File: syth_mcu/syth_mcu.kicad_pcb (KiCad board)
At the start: 2 copper layers, 138 x 121 mm, 33 parts, among them J1 USB_C_Receptacle_PowerOnly_6P, J2 Conn_01x05, J3 Conn_01x05, SW1 SW_Push, SW2 SW_Push, SW3 SW_Push, SW4 SW_Push, SW5 SW_Push, U1 TFT_320x240, U2 YAAJ_WeAct_BlackPill_Part_Like, U3 74HC4051, U4 AMS1117-3.3, U5 AMS1117-3.3

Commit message: kicad: widen board for 12-key hall row, wire DAC power, footprint fixes
- Edge.Cuts resized 167x94.5 -> 286x133mm to fit 12 real-pitch (23mm)
  hall-effect key positions below the control row
- H1-H12 mounting holes shifted to new bottom edge
- add dac-pchannel.kicad_sch as tracked sheet file (was external ref)
- C1/C2 footprint corrected to non-polarized box-film C_Rect
- misc footprint/placement fixes from Cream Bun review pass
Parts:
- added C1: 80nF, Capacitor_THT:CP_Radial_D4.0mm_P2.00mm, F.Cu at (211.7, 53.8)
- added C2: 80nF, Capacitor_THT:CP_Radial_D4.0mm_P2.00mm, F.Cu at (202.9, 70.4)
- added C3: 0.1uF C, Capacitor_THT:C_Disc_D5.0mm_W2.5mm_P2.50mm, F.Cu at (163.2, 69.4)
- added C4: 0.1uF C, Capacitor_THT:C_Disc_D5.0mm_W2.5mm_P2.50mm, F.Cu at (163.2, 62.9)
- added C5: 1uF, Capacitor_THT:C_Rect_L9.0mm_W3.2mm_P7.50mm_MKT, F.Cu at (209.2, 28.4)
- added C6: 33uF, Capacitor_THT:CP_Radial_D4.0mm_P2.00mm, F.Cu at (216.7, 53.8)
- added C7: 1uF, Capacitor_THT:C_Rect_L9.0mm_W3.2mm_P7.50mm_MKT, F.Cu at (167.7, 64.9)
- added C8: 33uF, Capacitor_THT:CP_Radial_D4.0mm_P2.00mm, F.Cu at (216.2, 75.3)
- added J4: AudioPlug3, Connector_Audio:Jack_3.5mm_CUI_SJ1-3533NG_Horizontal, F.Cu at (229.2, 26.1)
- added Q1: SI2307DS, Package_TO_SOT_SMD:SOT-23, F.Cu at (217.3, 37.8)
- added Q2: SI2304DS, Package_TO_SOT_SMD:SOT-23, F.Cu at (211.7, 37.6)
- added Q3: SI2307DS, Package_TO_SOT_SMD:SOT-23, F.Cu at (215.7, 67.9)
- added Q4: SI2304DS, Package_TO_SOT_SMD:SOT-23, F.Cu at (215.7, 63.1)
- added R10: 10k, Resistor_THT:R_Axial_DIN0207_L6.3mm_D2.5mm_P10.16mm_Horizontal, F.Cu at (211.9, 78.4)
- added R3: 10k, Resistor_THT:R_Axial_DIN0207_L6.3mm_D2.5mm_P10.16mm_Horizontal, F.Cu at (205.7, 42.9)
- added R4: 10k, Resistor_THT:R_Axial_DIN0207_L6.3mm_D2.5mm_P10.16mm_Horizontal, F.Cu at (210.7, 60.4)
- added R5: 2k, Resistor_THT:R_Axial_DIN0207_L6.3mm_D2.5mm_P10.16mm_Horizontal, F.Cu at (202.2, 32.7)
- added R6: 2k, Resistor_THT:R_Axial_DIN0207_L6.3mm_D2.5mm_P10.16mm_Horizontal, F.Cu at (209.2, 32.8)
- added R7: 100 1%, Resistor_THT:R_Axial_DIN0207_L6.3mm_D2.5mm_P10.16mm_Horizontal, F.Cu at (209.2, 43.8)
- added R8: 100 1%, Resistor_THT:R_Axial_DIN0207_L6.3mm_D2.5mm_P10.16mm_Horizontal, F.Cu at (211.9, 74.8)
- added R9: 10k, Resistor_THT:R_Axial_DIN0207_L6.3mm_D2.5mm_P10.16mm_Horizontal, F.Cu at (209.2, 47.8)
- added RV6: 100k, Potentiometer_THT:Potentiometer_Bourns_3296W_Vertical, F.Cu at (203.3, 47.3)
- added RV7: 100k, Potentiometer_THT:Potentiometer_Bourns_3296W_Vertical, F.Cu at (203.3, 58.3)
- U5: renamed from U1; moved to B.Cu
- moved R2 131.5 mm to (168.4, 29.6), turned to -90 degrees
- moved R1 125.3 mm to (162.9, 29.6), turned to -90 degrees
- moved D1 124.0 mm to (165.9, 25.3), turned to 0 degrees
- moved H11 122.2 mm to (284.7, 144.5)
- moved J1 116.4 mm to (292.7, 60.8)
- moved H9 106.7 mm to (260.6, 144.5)
- moved J3 106.2 mm to (20.0, 25.5), turned to 180 degrees
- moved U3 102.3 mm to (165.6, 47.5), turned to 180 degrees
- moved H7 91.3 mm to (236.4, 144.5)
- moved U4 87.9 mm to (165.6, 56.8), turned to 180 degrees
- moved H5 75.9 mm to (212.2, 144.5)
- moved U6 74.6 mm to (194.0, 78.0)
- moved H12 60.6 mm to (188.0, 144.5)
- moved H2 57.5 mm to (18.7, 144.5)
- moved J2 55.1 mm to (10.7, 60.8)
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- renumbered H7 to H10, H12 to H11, H8 to H12, H9 to H5, H5 to H6, H10 to H7, H6 to H8, H11 to H9, J3 to J1, J1 to J3, R3 to R1, R4 to R2, U4 to U3, U5 to U4, U3 to U6
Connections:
- U2 pad 11: unconnected-(U2-PB3-Pad11) -> PB3
- U2 pad 32: unconnected-(U2-PA6-Pad32) -> PA6
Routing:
- net GND: track 448.8 -> 0.00 mm, vias 3 -> 0
- net AMS1_3.3V: track 254.4 -> 0.00 mm, vias 1 -> 0
- net D_5V: track 220.0 -> 0.00 mm, vias 3 -> 0
- net PA0: track 172.2 -> 0.00 mm
- net PA1: track 164.2 -> 0.00 mm
- net PB7: track 157.9 -> 0.00 mm
- net PA2: track 150.3 -> 0.00 mm
- net PB6: track 147.7 -> 0.00 mm, vias 1 -> 0
- net PB2: track 145.6 -> 0.00 mm, vias 1 -> 0
- net PA3: track 142.3 -> 0.00 mm
- net PB4: track 124.7 -> 0.00 mm, vias 1 -> 0
- net PA11: track 115.4 -> 0.00 mm
- net PB1: track 113.7 -> 0.00 mm
- net PB0: track 108.7 -> 0.00 mm
- net AMS2_3.3V: track 94.6 -> 0.00 mm, vias 1 -> 0
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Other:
- board size 138 x 121 mm -> 286 x 133 mm

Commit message: update layout
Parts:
- removed H1, H2, H3, H4, H5: ~, Package_TO_SOT_THT:TO-92_Inline
- removed U6: 74HC4051, Package_DIP:DIP-16_W7.62mm
- added J5: Conn_01x20, Connector_PinSocket_2.54mm:PinSocket_1x20_P2.54mm_Vertical, F.Cu at (252.4, 22.8)
- added J6: Conn_01x20, Connector_PinSocket_2.54mm:PinSocket_1x20_P2.54mm_Vertical, F.Cu at (281.6, 22.8)
- added J7: Conn_01x16, Connector_PinSocket_2.54mm:PinSocket_1x16_P2.54mm_Vertical, B.Cu at (277.4, 101.3)
- added J8: Conn_01x08, Connector_PinSocket_2.54mm:PinSocket_1x08_P2.54mm_Vertical, B.Cu at (277.4, 80.2)
- added J9: Conn_01x07, Connector_PinSocket_2.54mm:PinSocket_1x07_P2.54mm_Vertical, F.Cu at (187.5, 102.4)
- SW1, SW2, SW3, SW4, SW5: footprint Button_Switch_THT:SW_PUSH_6mm -> Button_Switch_Keyboard:SW_Cherry_MX_1.00u_PCB
- U5: footprint YAAJ_Pills:TFT-320x240 -> Connector_PinHeader_2.54mm:PinHeader_1x14_P2.54mm_Vertical; moved to F.Cu
- moved J3 187.0 mm to (207.0, 25.9)
- moved J2 170.9 mm to (160.6, 143.0), turned to 0 degrees
- moved H6 149.9 mm to (265.2, 138.0)
- moved RV1 142.9 mm to (162.9, 26.8), turned to 0 degrees
- moved SW1 122.4 mm to (154.3, 68.8), turned to -90 degrees
- moved RV2 117.9 mm to (162.9, 44.6), turned to 0 degrees
- moved SW2 113.6 mm to (154.5, 49.8), turned to -90 degrees
- moved SW3 110.5 mm to (154.4, 30.7), turned to -90 degrees
- moved U4 108.7 mm to (224.0, -34.9)
- moved C3 97.7 mm to (238.5, 7.23)
- moved C8 97.0 mm to (228.5, -20.9), turned to 0 degrees
- moved H12 96.7 mm to (284.7, 144.5)
- moved C2 96.3 mm to (233.5, -20.9), turned to 0 degrees
- moved Q3 94.5 mm to (230.5, -25.4)
- moved R10 94.1 mm to (220.0, -15.3), turned to 90 degrees
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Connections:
- C1 pad 2: GND -> ENN
- C2 pad 2: GND -> ENN
- C3 pad 2: GND -> ENN
- C4 pad 2: GND -> ENN
- C5 pad 2: GND -> ENN
- C7 pad 2: GND -> ENN
- H10 pad 1: AMS1_3.3V -> ENN
- H10 pad 2: GND -> AMS1_3.3V
- H10 pad 3: Net-(H10-OUT) -> C9
- H11 pad 1: AMS1_3.3V -> ENN
- H11 pad 2: GND -> AMS1_3.3V
- H11 pad 3: PA3 -> C10
- H12 pad 1: AMS1_3.3V -> ENN
- H12 pad 2: GND -> AMS1_3.3V
- H12 pad 3: Net-(H12-OUT) -> C11
- H6 pad 2: GND -> ENN
- H6 pad 3: Net-(H6-OUT) -> C5
- H7 pad 2: GND -> ENN
- H7 pad 3: PA1 -> C6
- H8 pad 2: GND -> ENN
- H8 pad 3: Net-(H8-OUT) -> C7
- H9 pad 1: AMS1_3.3V -> ENN
- H9 pad 2: GND -> AMS1_3.3V
- H9 pad 3: PA2 -> C8
- J1 pad 2: GND -> ENN
- J2 pad 2: GND -> ENN
- J3 pad A12: GND -> ENN
- J3 pad B12: GND -> ENN
- J4 pad S: GND -> ENN
- Q2 pad 3: GND -> ENN
- Q4 pad 3: GND -> ENN
- R1 pad 2: GND -> ENN
- R10 pad 1: GND -> ENN
- R2 pad 2: GND -> ENN
- R3 pad 1: GND -> ENN
- R4 pad 1: GND -> ENN
- R4 pad 2: PA6 -> PA15
- R6 pad 1: PA6 -> PA15
- R9 pad 1: GND -> ENN
- RV1 pad 3: GND -> ENN
- RV2 pad 3: GND -> ENN
- RV3 pad 3: GND -> ENN
- RV4 pad 3: GND -> ENN
- RV5 pad 3: GND -> ENN
- RV6 pad 3: GND -> ENN
- RV7 pad 3: GND -> ENN
- SW1 pad 1: GND -> ENN
- SW2 pad 1: GND -> ENN
- SW3 pad 1: GND -> ENN
- SW4 pad 1: GND -> ENN
- SW5 pad 1: GND -> ENN
- U2 pad 10: unconnected-(U2-PA15-Pad10) -> PA15
- U2 pad 18: unconnected-(U2-5V-Pad18) -> D_5V
- U2 pad 19: unconnected-(U2-GND-Pad19) -> ENN
- U2 pad 2: unconnected-(U2-PB13-Pad2) -> PB13
- U2 pad 20: unconnected-(U2-3V3-Pad20) -> 3V3
- U2 pad 21: unconnected-(U2-VBat-Pad21) -> VBat
- U2 pad 22: unconnected-(U2-PC13-Pad22) -> PC13
- U2 pad 23: unconnected-(U2-PC14-Pad23) -> PC14
- U2 pad 24: unconnected-(U2-PC15-Pad24) -> PC15
- U2 pad 25: unconnected-(U2-RES-Pad25) -> RES
- U2 pad 3: unconnected-(U2-PB14-Pad3) -> PB14
- U2 pad 37: unconnected-(U2-PB10-Pad37) -> PB10
- U2 pad 38: unconnected-(U2-3V3-Pad38) -> 3V3
- U2 pad 39: GND -> ENN
- U2 pad 4: unconnected-(U2-PB15-Pad4) -> PB15
- U3 pad 1: GND -> ENN
- U4 pad 1: GND -> ENN
- U5 pad 2: GND -> ENN
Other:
- board size 286 x 133 mm -> 100 x 100 mm

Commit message: update layout
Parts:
- moved SW4 120.7 mm to (275.2, 100.5), turned to 0 degrees
- moved RV5 104.6 mm to (267.3, 89.0), turned to 90 degrees
- moved SW5 102.3 mm to (256.1, 100.6), turned to 0 degrees
- moved C4 89.7 mm to (168.2, 66.9)
- moved C7 89.7 mm to (165.5, 67.2)
- moved C1 89.7 mm to (166.5, 55.2)
- moved C2 89.7 mm to (166.5, 38.7)
- moved C3 89.7 mm to (171.5, 66.9)
- moved C5 89.7 mm to (164.5, 26.7)
- moved C6 89.7 mm to (166.5, 49.2)
- moved C8 89.7 mm to (161.5, 38.7)
- moved Q2 89.7 mm to (167.0, 59.7)
- moved Q3 89.7 mm to (163.5, 34.2)
- moved Q4 89.7 mm to (167.6, 34.2)
- moved R10 89.7 mm to (153.0, 44.3)
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
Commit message: update layout
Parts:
- added G***: LOGO, LOGO, F.Cu at (122.1, 96.4)
- J7, J8: moved to F.Cu
- U5: footprint Connector_PinHeader_2.54mm:PinHeader_1x14_P2.54mm_Vertical -> Connector_PinSocket_2.54mm:PinSocket_1x14_P2.54mm_Vertical
- moved H6 154.7 mm to (111.2, 123.4)
- moved J9 134.1 mm to (104.0, 125.9)
- moved J7 113.4 mm to (140.1, 52.9), turned to 0 degrees
- moved RV7 106.5 mm to (149.7, 100.1), turned to 0 degrees
- moved H12 96.9 mm to (190.2, 123.4)
- moved J4 94.1 mm to (133.0, 51.4)
- moved J5 92.5 mm to (165.0, 52.9)
- moved J6 92.5 mm to (194.2, 52.9)
- moved U2 92.3 mm to (172.0, 53.0)
- moved Q1 92.3 mm to (160.8, 91.4)
- moved RV6 90.3 mm to (160.5, 100.1), turned to 0 degrees
- moved D1 88.8 mm to (118.9, 62.5)
- moved R1 88.8 mm to (122.5, 60.1)
- moved R2 88.8 mm to (125.9, 60.1)
- moved J3 88.6 mm to (122.2, 51.4)
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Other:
- board text added: "67011178 Napaul I. 67011214 Nuttawee W. 67011220 Pacharapol P. 67011246 Pavikan B. 67011594 Chuthathip T. 67011671 Tithipan T."
- board text added: "V1.0"

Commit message: update layout
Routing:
- net ENN: track 0.00 -> 453.4 mm, vias 0 -> 1
- net D_5V: track 0.00 -> 242.0 mm, vias 0 -> 4
- net AMS1_3.3V: track 0.00 -> 240.9 mm, vias 0 -> 1
- net AMS2_3.3V: track 0.00 -> 130.5 mm
- net PB6: track 0.00 -> 121.0 mm
- net PB7: track 0.00 -> 118.6 mm
- net PA0: track 0.00 -> 100.3 mm, vias 0 -> 2
- net C11: track 0.00 -> 93.6 mm, vias 0 -> 1
- net PB5: track 0.00 -> 90.0 mm, vias 0 -> 1
- net C0: track 0.00 -> 89.1 mm
- net PA7: track 0.00 -> 88.8 mm
- net C4: track 0.00 -> 88.8 mm
- net PA11: track 0.00 -> 88.7 mm, vias 0 -> 1
- net C1: track 0.00 -> 88.5 mm
- net C2: track 0.00 -> 88.4 mm
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
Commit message: update layout
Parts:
- removed U2: YAAJ_WeAct_BlackPill_Part_Like, YAAJ_Pills:YAAJ_WeAct_BlackPill_2
- added J10: Conn_01x20, Connector_PinSocket_2.54mm:PinSocket_1x20_P2.54mm_Vertical, F.Cu at (169.2, 52.9)
- added J11: Conn_01x20, Connector_PinSocket_2.54mm:PinSocket_1x20_P2.54mm_Vertical, F.Cu at (191.2, 52.9)
- C5, C7: footprint Capacitor_THT:C_Rect_L9.0mm_W3.2mm_P7.50mm_MKT -> Capacitor_THT:CP_Radial_D5.0mm_P2.00mm
- J5, J6: footprint Connector_PinSocket_2.54mm:PinSocket_1x20_P2.54mm_Vertical -> Connector_PinHeader_2.54mm:PinHeader_1x20_P2.54mm_Vertical
- moved SW1 38.2 mm to (117.9, 128.4)
- moved SW3 38.2 mm to (156.2, 128.4)
- moved SW4 19.1 mm to (175.3, 128.4)
- moved SW5 19.1 mm to (194.4, 128.4)
- moved J9 14.4 mm to (103.9, 140.3), turned to 180 degrees
- moved C5 3.61 mm to (149.9, 78.4), turned to -90 degrees
- moved C4 2.30 mm to (161.4, 52.2)
- moved R8 2.13 mm to (149.6, 63.9)
- moved C7 1.86 mm to (145.2, 64.0)
- moved J6 1.10 mm to (195.3, 52.9)
- moved U4 0.60 mm to (148.7, 55.7)
- moved J7 0.30 mm to (140.1, 53.2)
- moved J8 0.30 mm to (161.1, 60.9)
- moved C8 0.20 mm to (156.0, 53.2)
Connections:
- J7 pad 1: C0 -> C15
- J7 pad 10: C9 -> C6
- J7 pad 11: C10 -> C5
- J7 pad 12: C11 -> C4
- J7 pad 13: C12 -> C3
- J7 pad 14: C13 -> C2
- J7 pad 15: C14 -> C1
- J7 pad 16: C15 -> C0
- J7 pad 2: C1 -> C14
- J7 pad 3: C2 -> C13
- J7 pad 4: C3 -> C12
- J7 pad 5: C4 -> C11
- J7 pad 6: C5 -> C10
- J7 pad 7: C6 -> C9
- J7 pad 8: C7 -> C8
- J7 pad 9: C8 -> C7
- J8 pad 1: PB15 -> PB0
- J8 pad 5: PB0 -> PB15
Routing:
- net ENN: track 453.4 -> 0.00 mm, vias 1 -> 0
- net D_5V: track 242.0 -> 0.00 mm, vias 4 -> 0
- net AMS1_3.3V: track 240.9 -> 0.00 mm, vias 1 -> 0
- net AMS2_3.3V: track 130.5 -> 0.00 mm
- net PB6: track 121.0 -> 0.00 mm
- net PB7: track 118.6 -> 0.00 mm
- net PA0: track 100.3 -> 0.00 mm, vias 2 -> 0
- net C11: track 93.6 -> 0.00 mm, vias 1 -> 0
- net PB5: track 90.0 -> 0.00 mm, vias 1 -> 0
- net C0: track 89.1 -> 0.00 mm
- net PA7: track 88.8 -> 0.00 mm
- net C4: track 88.8 -> 0.00 mm
- net PA11: track 88.7 -> 0.00 mm, vias 1 -> 0
- net C1: track 88.5 -> 0.00 mm
- net C2: track 88.4 -> 0.00 mm
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- added copper zone on B.Cu, net ENN
- added copper zone on F.Cu, net ENN

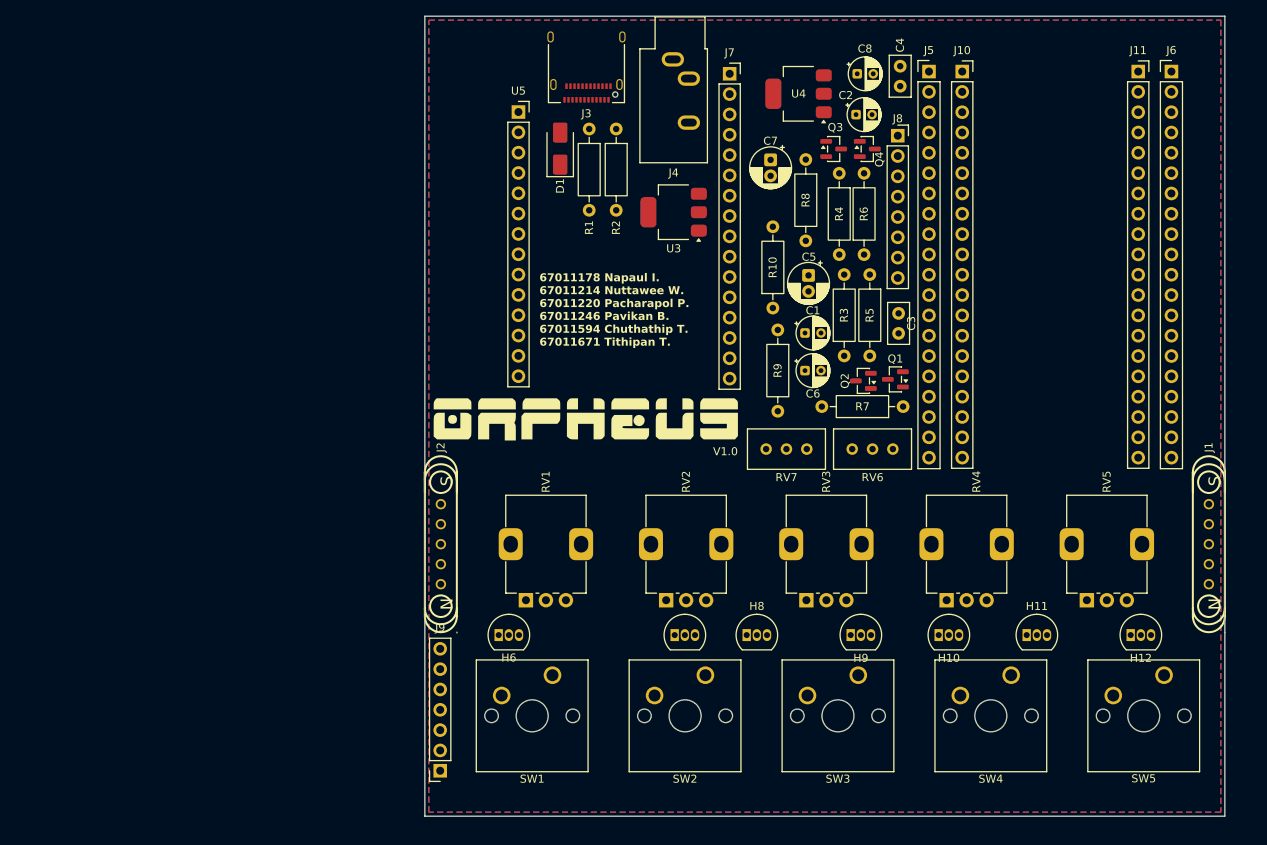
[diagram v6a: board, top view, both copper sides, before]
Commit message: synth: fix 3D models, source real jack part, rename syth big -> syth_mcu
3D model fixes (all footprints were pointing at broken/missing paths):
- Pot (RV1-7): Alps RK09K STEP wired via project-relative ${KIPRJMOD} path
- Pogo connector (J1/J2): real magnetic pogo STEP, replaced broken
  pogo5.3dshapes reference that pointed at a folder that never existed
- Switch (SW1-6): sourced Kailh LP Choc STEP + MX-Alps-Choc-1U hybrid
  footprint (drop-in candidate for existing Cherry MX pad pattern)
- Jack (J4): sourced real, cheap (~35 THB), Thailand-buyable PJ-316 part
  via easyeda2kicad (LCSC C2884936) - symbol, footprint, and 3D model
  all pulled fresh

All models now use ${KIPRJMOD}-relative paths under syth_mcu/local_3dmodels/
so they resolve on any machine after git pull, not just this one.

Also folds in the syth big -> syth_mcu folder rename and other pending
schematic/production file changes.
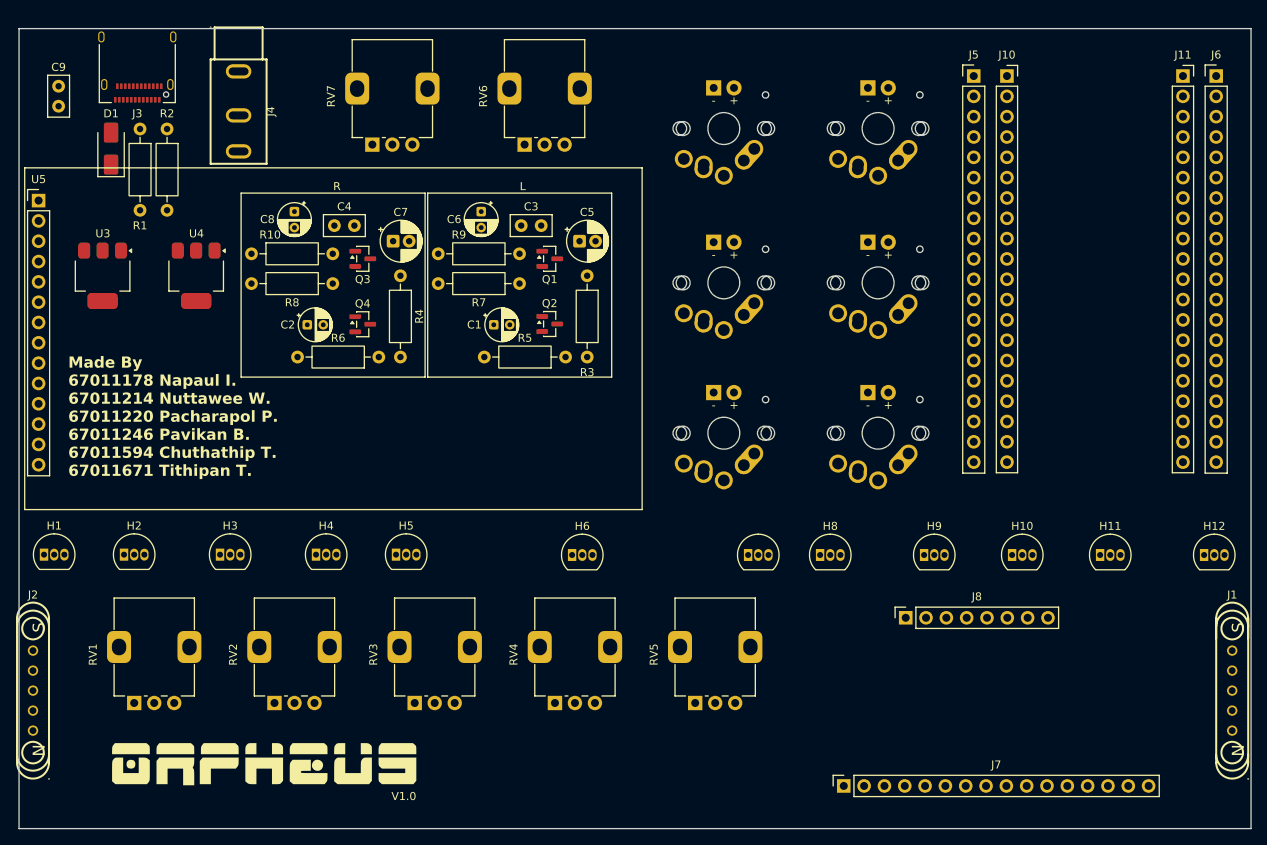
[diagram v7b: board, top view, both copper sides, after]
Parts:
- removed J9: Conn_01x07, Connector_PinSocket_2.54mm:PinSocket_1x07_P2.54mm_Vertical
- added C9: C_Small, Capacitor_THT:C_Disc_D5.0mm_W2.5mm_P2.50mm, F.Cu at (56.2, 54.8)
- added H1: ~, Package_TO_SOT_THT:TO-92_Inline, F.Cu at (54.4, 113.3)
- added H2: ~, Package_TO_SOT_THT:TO-92_Inline, F.Cu at (64.4, 113.3)
- added H3: ~, Package_TO_SOT_THT:TO-92_Inline, F.Cu at (76.4, 113.3)
- added H4: ~, Package_TO_SOT_THT:TO-92_Inline, F.Cu at (88.4, 113.3)
- added H5: ~, Package_TO_SOT_THT:TO-92_Inline, F.Cu at (98.4, 113.3)
- added SW6: SW_Push, synth:MX-Alps-Choc-1U, F.Cu at (139.4, 98.1)
- D1: value SS14 -> SS34
- J4: footprint Connector_Audio:Jack_3.5mm_CUI_SJ1-3533NG_Horizontal -> synth:CONN-TH_PJ-316
- RV1, RV2, RV3, RV4, RV5: footprint Potentiometer_THT:Potentiometer_Alps_RK09K_Single_Vertical -> synth:Potentiometer_Alps_RK09K_Single_Vertical
- RV6, RV7: footprint Potentiometer_THT:Potentiometer_Bourns_3296W_Vertical -> synth:Potentiometer_Alps_RK09K_Single_Vertical
- SW1, SW2, SW3, SW4, SW5: footprint Button_Switch_Keyboard:SW_Cherry_MX_1.00u_PCB -> synth:MX-Alps-Choc-1U
- U5: footprint Connector_PinSocket_2.54mm:PinSocket_1x14_P2.54mm_Vertical -> Connector_PinHeader_2.54mm:PinHeader_1x14_P2.54mm_Vertical
- moved J7 90.2 mm to (154.3, 142.2), turned to 90 degrees
- moved U4 78.7 mm to (73.4, 78.5), turned to -90 degrees
- moved C2 73.5 mm to (87.3, 84.6)
- moved C8 72.4 mm to (85.7, 70.4), turned to -90 degrees
- moved U3 71.8 mm to (61.7, 78.5), turned to -90 degrees
- moved SW2 71.7 mm to (158.6, 60.0), turned to 180 degrees
- moved SW1 71.6 mm to (139.4, 60.0), turned to 180 degrees
- moved C4 71.1 mm to (93.2, 72.2), turned to 180 degrees
- moved Q4 66.8 mm to (94.2, 84.5)
- moved RV7 66.3 mm to (95.4, 62.0), turned to 90 degrees
- moved R10 65.5 mm to (80.3, 75.7), turned to 0 degrees
- moved R6 62.0 mm to (96.2, 88.6), turned to 180 degrees
- moved R8 61.1 mm to (90.5, 79.4), turned to 180 degrees
- moved U5 61.0 mm to (53.7, 69.0)
- moved Q3 60.4 mm to (94.2, 76.3)
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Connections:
- C1 pad 2: ENN -> GND
- C2 pad 2: ENN -> GND
- C3 pad 2: ENN -> GND
- C4 pad 2: ENN -> GND
- C5 pad 2: ENN -> GND
- C7 pad 2: ENN -> GND
- H10 pad 1: ENN -> AMS1_3.3V
- H10 pad 2: AMS1_3.3V -> GND
- H11 pad 1: ENN -> AMS1_3.3V
- H11 pad 2: AMS1_3.3V -> GND
- H12 pad 1: ENN -> AMS1_3.3V
- H12 pad 2: AMS1_3.3V -> GND
- H6 pad 2: ENN -> GND
- H7 pad 2: ENN -> GND
- H8 pad 2: ENN -> GND
- H9 pad 1: ENN -> AMS1_3.3V
- H9 pad 2: AMS1_3.3V -> GND
- J1 pad 2: ENN -> GND
- J1 pad 5: PA12 -> GND
- J10 pad 19: ENN -> GND
- J11 pad 2: ENN -> GND
- J2 pad 2: ENN -> GND
- J2 pad 5: PA11 -> GND
- J3 pad A12: ENN -> GND
- J3 pad B12: ENN -> GND
- J3 pad SH: unconnected-(J3-SHIELD-PadSH)_1 -> Net-(J3-SHIELD)
- J5 pad 19: ENN -> GND
- J6 pad 2: ENN -> GND
- J8 pad 1: PB0 -> PB5
- J8 pad 2: PB14 -> PB0
- J8 pad 3: PB13 -> PB2
- J8 pad 4: PB2 -> PB1
- J8 pad 5: PB15 -> PB10
- J8 pad 6: ENN -> GND
- J8 pad 8: ENN -> GND
- Q2 pad 3: ENN -> GND
- Q4 pad 3: ENN -> GND
- R1 pad 2: ENN -> GND
- R10 pad 1: ENN -> GND
- R2 pad 2: ENN -> GND
- R3 pad 1: ENN -> GND
- R4 pad 1: ENN -> GND
- R9 pad 1: ENN -> GND
- RV1 pad 3: ENN -> GND
- RV2 pad 3: ENN -> GND
- RV3 pad 3: ENN -> GND
- RV4 pad 3: ENN -> GND
- RV5 pad 3: ENN -> GND
- RV6 pad 3: ENN -> GND
- RV7 pad 3: ENN -> GND
- SW1 pad 1: ENN -> GND
- SW1 pad 2: PB4 -> PB12
- SW2 pad 1: ENN -> GND
- SW2 pad 2: PB5 -> PB15
- SW3 pad 1: ENN -> GND
- SW3 pad 2: PB8 -> PB4
- SW4 pad 1: ENN -> GND
- SW4 pad 2: PB9 -> PB5
- SW5 pad 1: ENN -> GND
- SW5 pad 2: PB12 -> PB8
- U3 pad 1: ENN -> GND
- U4 pad 1: ENN -> GND
- U5 pad 2: ENN -> GND
- U5 pad 6: PA7 -> PB14
- U5 pad 7: PA5 -> PB13
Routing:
- removed copper zone on B.Cu, net ENN
- removed copper zone on F.Cu, net ENN
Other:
- board size 100 x 100 mm -> 154 x 100 mm
- board text added: "L"
- board text added: "Made By 67011178 Napaul I. 67011214 Nuttawee W. 67011220 Pacharapol P. 67011246 Pavikan B. 67011594 Chuthathip T. 67011671 Tithipan T."
- board text added: "R"
- board text removed: "67011178 Napaul I. 67011214 Nuttawee W. 67011220 Pacharapol P. 67011246 Pavikan B. 67011594 Chuthathip T. 67011671 Tithipan T."
